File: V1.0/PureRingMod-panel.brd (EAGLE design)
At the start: 128.5 x 60.3 mm, 27 parts

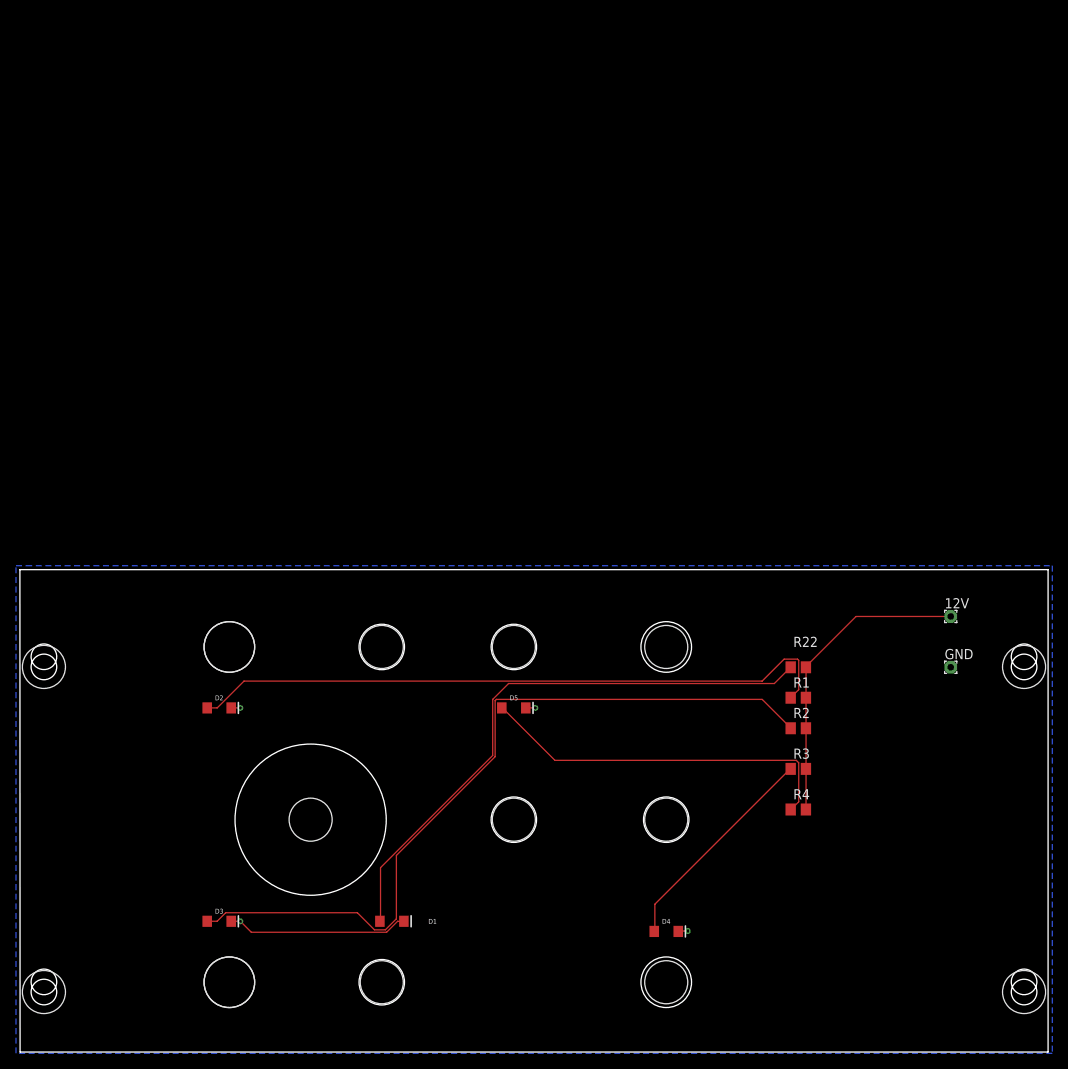
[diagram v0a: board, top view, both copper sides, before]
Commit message: Panel layout and routing
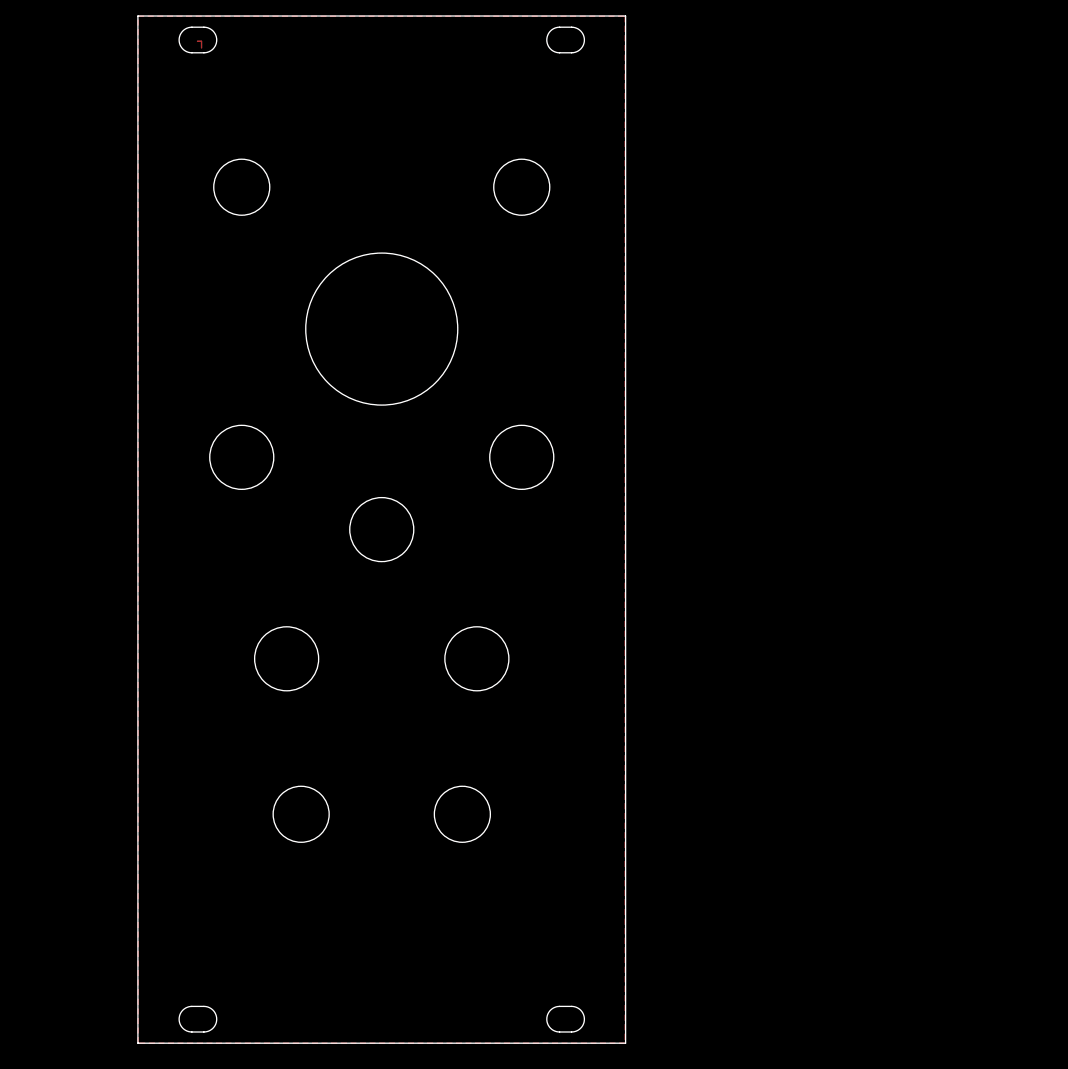
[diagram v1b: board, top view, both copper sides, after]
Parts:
- removed 12V: 12V pad, wirepad:1,6/0,8
- removed D1, D2, D3, D4, D5: BLUE, SparkFun-LED:LED-1206
- removed GND: GND Pad, wirepad:1,6/0,8
- removed R1, R2, R22, R3, R4: 330, rcl:R0805
- removed U$1, U$3: S_JACK_PANEL, GMSN-R2Project:S_JACK_PANEL
- removed U$10, U$6, U$7, U$8, U$9: POT_PANEL, GMSN-R2Project:POT_PANEL
- removed U$11: XLR_PANEL, GMSN-R2Project:XLR_PANEL
- removed U$12, U$13, U$14, U$15: MOUNTING_HOLE, GMSN-R2Project:MOUNTING_HOLE
- removed U$2: (no value), gmsnLogo:GMSN!_LOGO
- removed U$4, U$5: S_JACK_PANEL, GMSN-R2Project:S_JACK_PANEL@1
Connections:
- removed net 12V: 12V.1, R1.2, R2.2, R22.2, R3.2, R4.2
- removed net GND: D1.C, D2.C, D3.C, D4.C, D5.C, GND.1
- removed net N$1: D1.A, R22.1
- removed net N$3: D2.A, R1.1
- removed net N$5: D3.A, R2.1
- removed net N$7: D4.A, R3.1
- removed net N$9: D5.A, R4.1
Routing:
- net N$5: track 96.5 -> 0.00 mm
- net N$3: track 81.6 -> 0.00 mm
- net N$1: track 72.5 -> 1.37 mm
- net N$9: track 46.2 -> 0.00 mm
- net 12V: track 38.6 -> 0.00 mm
- net N$7: track 27.4 -> 0.00 mm
- net GND: track 26.3 -> 0.00 mm, vias 4 -> 0
- added copper zone on layer 1, net GND
- removed copper zone on layer 16, net GND
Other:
- board size 128.5 x 60.3 mm -> 61 x 128.4 mm
- board text removed: "CC BY 3.0"
- board text removed: "Carrier"
- board text removed: "Carrier Volume"
- board text removed: "Gain"
- board text removed: "Mic In"
- board text removed: "Mic Mix"
- board text removed: "Mix"
- board text removed: "Modulator"
- board text removed: "Modulator Volume"
- board text removed: "Output"
- board text removed: "Output 2"
- board text removed: "Pure Ring Modulator"
- board text removed: "Ring Modulator Design Andy C From a design by Roman Sowa"
- board text removed: "V1.0"
